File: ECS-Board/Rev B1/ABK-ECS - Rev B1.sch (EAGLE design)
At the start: 247 parts, among them J10 22-05-7068-06, J11 FTSH-105-01-L-DV-NOPASTE, J2 USB-B-S-RA, J21 FTSH-103-01-L-DV-NOPASTE, J4 MSTBA2, J5 22-05-7068-06, J6 22-05-7028-02, J7 22-05-7068-06, J8 22-05-7068-06, J9 22-05-7028-02, K1 G6K-2G-Y, SW1 B3FS-1015, SW2 B3FS-1015, T1 EXMACHINA-LOGO-NAME, T10 MMBT2222AL, T11 MMBT2222AL, T12 IRLML5103TRPBF, T13 IRLML5103TRPBF, T14 IRLML5103TRPBF, T15 IRLML5103TRPBF, T16 MMBT2222AL, T17 MMBT2222AL, T18 MMBT2222AL, T19 MMBT2222AL, T2 IRLML5103TRPBF, T20 MMBT2907ALT3, T3 MMBT2222AL, T4 IRLML5103TRPBF, T5 IRLML5103TRPBF, T6 IRLML5103TRPBF, T7 IRLML5103TRPBF, T8 MMBT2222AL, T9 MMBT2222AL, U1 AT24C512C-SSHM-B, U2 LPC1768FBD100, U3 LT3686HDDPBF, U4 LT3686HDDPBF, U6 CD4050BD, U7 CD4050BD, X1 FC-135, X2 ASE-12, X3 3000

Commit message: Place and route ethernet interface
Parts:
- removed D14: 1N4148WS, diode:1N4148WS
- removed J21: FTSH-103-01-L-DV-NOPASTE, con-samtec:FTSH-103-01-L-DV-NOPASTE
- added C20, C21: 0.1uF, rcl:C-EUC0603
- added C25, C27, C28, C29, C31, C32, C33, C34: 100nF, rcl:C-EUC0603
- added C26, C30: 10uF, rcl:CPOL-EUCT3216
- added D4: STPS3L40UF, diode:STPS3L40UF
- added J1: USB-B-S-RA, con-multicomp:USB-B-S-RA
- added J12: RB1-125BAG1A, con-wiznet:RB1-125BAG1A
- added J3: 22-05-7068-06, con-molex:22-05-7068-06
- added R124, R125: 220, rcl:R-EU_R0603
- added R126, R127, R128, R129: 49.9, rcl:R-EU_R0603
- added R130: 4K7, rcl:R-EU_R0603
- added R131: 2K2, rcl:R-EU_R0603
- added U5: CD4050BD, ti:CD4050BD
- added X4: ASE_50, crystal:ASE
- C1: value 10uF -> 0.1uF; device rcl:CPOL-EUCT3216 -> rcl:C-EUC0603; MPN F931A106MAA -> MC0603B104K160CT; OC_NEWARK 58R3260 -> 06R4923
- C10, C5: value 18pF -> 0.1uF; MPN GRM1885C1H180JA01D -> MC0603B104K160CT; OC_NEWARK 14T3328 -> 06R4923
- C23: value 0.1uF -> 4.7uF; device rcl:C-EUC0603 -> rcl:CPOL-EUCT3216; MPN MC0603B104K160CT -> F931A475MAA; OC_NEWARK 06R4923 -> 58R3271
- C24: value 0.1uF -> 100nF; MPN MC0603B104K160CT -> MC0603B104K250CT; OC_NEWARK 06R4923 -> 06R4925
- C3, C9: value 0.1uF -> 18pF; MPN MC0603B104K160CT -> GRM1885C1H180JA01D; OC_NEWARK 06R4923 -> 14T3328
- C4: value 0.1uF -> 10uF; device rcl:C-EUC0603 -> rcl:CPOL-EUCT3216; MPN MC0603B104K160CT -> F931A106MAA; OC_NEWARK 06R4923 -> 58R3260
- D5: value STPS3L40UF -> 1N4148WS; device diode:STPS3L40UF -> diode:1N4148WS; MPN (none) -> 1N4148WS; OC_NEWARK 06X0873 -> 31Y5518
- J10: value 22-05-7068-06 -> FTSH-105-01-L-DV-NOPASTE; device con-molex:22-05-7068-06 -> con-samtec:FTSH-105-01-L-DV-NOPASTE
- J11: value FTSH-105-01-L-DV-NOPASTE -> 22-05-7028-02; device con-samtec:FTSH-105-01-L-DV-NOPASTE -> con-molex:22-05-7028-02; MPN (none) -> 22-05-7028; OC_NEWARK (none) -> 25M1728
- J2: value USB-B-S-RA -> MSTBA2; device con-multicomp:USB-B-S-RA -> con-phoenix-508:MSTBA2; MPN USB-B-S-RA -> (none); OC_NEWARK 14N8154 -> (none)
- J4: value MSTBA2 -> 22-05-7028-02; device con-phoenix-508:MSTBA2 -> con-molex:22-05-7028-02; MPN (none) -> 22-05-7028; OC_NEWARK (none) -> 25M1728
- J6: value 22-05-7028-02 -> 22-05-7068-06; device con-molex:22-05-7028-02 -> con-molex:22-05-7068-06; MPN 22-05-7028 -> (none); OC_NEWARK 25M1728 -> (none)
- J8: value 22-05-7068-06 -> 22-05-7028-02; device con-molex:22-05-7068-06 -> con-molex:22-05-7028-02; MPN (none) -> 22-05-7028; OC_NEWARK (none) -> 25M1728
- J9: value 22-05-7028-02 -> FTSH-103-01-L-DV-NOPASTE; device con-molex:22-05-7028-02 -> con-samtec:FTSH-103-01-L-DV-NOPASTE; MPN 22-05-7028 -> (none); OC_NEWARK 25M1728 -> (none)
- R5: value 1K -> 39K; device rcl:R-EU_R1206 -> rcl:R-EU_R0603
- R6: value 33 -> 24K; MPN RC0603FR-0733RL -> (none); OC_NEWARK 68R0085 -> (none)
- R64: value 10K -> 1K; device rcl:R-EU_R0603 -> rcl:R-EU_R1206; MPN RC0603FR-0710KL -> (none); OC_NEWARK 68R0049 -> (none)
- R65: value 100 -> 1K; device rcl:R-EU_R0603 -> rcl:R-EU_R1206; MPN RC0603FR-13100RL -> (none); OC_NEWARK 68R0131 -> (none)
- R67, R68, R69: value 1K -> 10K; device rcl:R-EU_R1206 -> rcl:R-EU_R0603; MPN (none) -> RC0603FR-0710KL; OC_NEWARK (none) -> 68R0049
- R71, R72, R73: value 10K -> 1K; MPN RC0603FR-0710KL -> RC0603FR-071KL; OC_NEWARK 68R0049 -> 68R0042
- R75, R76, R77: value 1K -> 1K5; MPN RC0603FR-071KL -> RC0603FR-071K5L; OC_NEWARK 68R0042 -> 68R0045
- R79, R80, R81: value 1K5 -> 4K7; MPN RC0603FR-071K5L -> RC0603FR-074K7L; OC_NEWARK 68R0045 -> 68R0092
- R8: value 24K -> 33; MPN (none) -> RC0603FR-0733RL; OC_NEWARK (none) -> 68R0085
- R83, R84, R85: value 4K7 -> 100; MPN RC0603FR-074K7L -> RC0603FR-13100RL; OC_NEWARK 68R0092 -> 68R0131
- R87, R88, R89: value 100 -> 330; MPN RC0603FR-13100RL -> RC0603FR-07330RL; OC_NEWARK 68R0131 -> 98K7391
- R91: value 330 -> 1K; device rcl:R-EU_R0603 -> rcl:R-EU_R1206; MPN RC0603FR-07330RL -> (none); OC_NEWARK 98K7391 -> (none)
- R92: value 330 -> 10K; MPN RC0603FR-07330RL -> RC0603FR-0710KL; OC_NEWARK 98K7391 -> 68R0049
- R93: value 330 -> 100; MPN RC0603FR-07330RL -> RC0603FR-13100RL; OC_NEWARK 98K7391 -> 68R0131
- R97: value 39K -> 1K; device rcl:R-EU_R0603 -> rcl:R-EU_R1206
- T1: value EXMACHINA-LOGO-NAME -> MMBT2907ALT3; device exmachina:EXMACHINA-LOGO-NAME -> transistor:MMBT2907ALT3; OC_NEWARK unknown -> (none)
- T11, T16, T3: value MMBT2222AL -> IRLML5103TRPBF; device transistor:MMBT2222AL -> International_Rectifier_By_element14_Batch_1:IRLML5103TRPBF; MF ON SEMICONDUCTOR -> INTERNATIONAL RECTIFIER(IR); MPN MMBT2222ALT1G -> IRLML5103TRPBF; OC_NEWARK 84K8795 -> 63J7612
- T12, T7: value IRLML5103TRPBF -> MMBT2222AL; device International_Rectifier_By_element14_Batch_1:IRLML5103TRPBF -> transistor:MMBT2222AL; MF INTERNATIONAL RECTIFIER(IR) -> ON SEMICONDUCTOR; MPN IRLML5103TRPBF -> MMBT2222ALT1G; OC_NEWARK 63J7612 -> 84K8795
- T2: value IRLML5103TRPBF -> EXMACHINA-LOGO-NAME; device International_Rectifier_By_element14_Batch_1:IRLML5103TRPBF -> exmachina:EXMACHINA-LOGO-NAME; MF INTERNATIONAL RECTIFIER(IR) -> (none); MPN IRLML5103TRPBF -> (none); OC_NEWARK 63J7612 -> unknown
- T20: value MMBT2907ALT3 -> MMBT2222AL; device transistor:MMBT2907ALT3 -> transistor:MMBT2222AL; MF (none) -> ON SEMICONDUCTOR; MPN (none) -> MMBT2222ALT1G; OC_NEWARK (none) -> 84K8795
- TC1: value TC2050-IDC-NL -> TC2030-IDC-NL; device TagConnect:TC2050-IDC-NL -> TagConnect:TC2030-IDC-NL
- TC2: value TC2030-IDC-NL -> TC2050-IDC-NL; device TagConnect:TC2030-IDC-NL -> TagConnect:TC2050-IDC-NL
- U7: value CD4050BD -> DP83848JSQ/NOPB; device ti:CD4050BD -> textas:DP83848JSQ/NOPB; MPN (none) -> DP83848JSQ/NOPB; OC_NEWARK (none) -> 96W2841
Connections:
- removed net N$75 (its old number): LED17.A, R74.1, R82.1, R86.1
- removed net N$76 (its old number): OK3A.EMIT, R86.2
- removed net N$79 (its old number): LED18.A, R75.1, R83.1, R87.1
- removed net N$80 (its old number): OK3B.EMIT, R87.2
- removed net N$83 (its old number): LED19.A, R76.1, R84.1, R88.1
- removed net N$86 (its old number): LED20.A, R77.1, R85.1, R89.1
- removed net N$87 (its old number): OK3C.EMIT, R88.2
- removed net N$88 (its old number): OK3D.EMIT, R89.2
- removed net N$89 (its old number): OK3A.A, R90.1
- removed net N$91 (its old number): OK3B.A, R91.1
- removed net N$92 (its old number): OK3D.A, R93.1
- removed net N$93 (its old number): OK3C.A, R92.1
- removed net N$94 (its old number): LED17.C, R78.1
- removed net N$95 (its old number): LED18.C, R79.1
- removed net N$96 (its old number): LED19.C, R80.1
- removed net N$97 (its old number): LED20.C, R81.1
- new net AGND: J12.P$1
- new net ETH_CRS: U2.P1[8]/ENET_CRS, U7.CRS/CRS_DV/LED_CFG
- new net ETH_MDC: U2.P1[16]/ENET_MDC, U7.MDC
- new net ETH_MDIO: U2.P1[17]/ENET_MDIO, U7.MDIO
- new net ETH_RST: U7.RESET_N
- new net ETH_RXD_0: U2.P1[9]/ENET_RXD0, U7.RXD_0/PHYAD1
- new net ETH_RXD_1: U2.P1[10]/ENET_RXD1, U7.RXD_1/PHYAD2
- new net ETH_RX_ER: U2.P1[14]/ENET_RX_ER, U7.RX_ER/MDIX_EN
- new net ETH_RX_N: J12.RD-, R129.2, U7.RD-
- new net ETH_RX_P: J12.RD+, R128.2, U7.RD+
- new net ETH_TXD_0: U2.P1[0]/ENET_TXD0, U7.TXD_0
- new net ETH_TXD_1: U2.P1[1]/ENET_TXD1, U7.TXD_1
- new net ETH_TXD_EN: U2.P1[4]/ENET_TX_EN, U7.TX_EN
- new net ETH_TX_N: J12.TD-, R127.2, U7.TD-
- new net ETH_TX_P: J12.TD+, R126.2, U7.TD+
- new net ETH_X1: U2.P1[15]/ENET_REF_CLK, U7.X1, X4.OUT
- new net L1_1: J12.L2, U7.LED_LINK/AN0
- new net L1_2: J12.L4, U7.LED_SPEED/AN1
- new net MII_MODE: R131.2, U7.RX_DV/MII_MODE
- new net N$113: J12.L1, R124.1
- new net N$115: J12.L3, R125.1
- new net N$116: R130.1, U7.RBIAS
- new net N$31: LED17.A, R71.1, R79.1, R83.1
- new net N$33: OK3A.EMIT, R83.2
- new net N$34: LED18.A, R72.1, R80.1, R84.1
- new net N$35: OK3B.EMIT, R84.2
- new net N$36: LED19.A, R73.1, R81.1, R85.1
- new net N$37: LED20.A, R74.1, R82.1, R86.1
- new net N$38: OK3C.EMIT, R85.2
- new net N$39: OK3D.EMIT, R86.2
- new net N$40: OK3A.A, R87.1
- new net N$42: OK3B.A, R88.1
- new net N$43: OK3D.A, R90.1
- new net N$46: OK3C.A, R89.1
- new net N$66: LED17.C, R75.1
- new net N$67: LED18.C, R76.1
- new net N$68: LED19.C, R77.1
- new net N$69: LED20.C, R78.1
- new net PFBOUT: C26.+, C27.1, C28.1, C29.1, U7.PFBIN1, U7.PFBIN2, U7.PFBOUT
- net !ISP_BOOT: now also J9-2.S, TC1.2; no longer J21-2.S, TC2.2
- net !ISP_RST: now also J9-6.S, TC1.6; no longer J21-6.S, TC2.6
- net !RESET: now also J10-10.S, TC2.10; no longer J11-10.S, TC1.10
- net +24V: now also J3-1.S, J4-1.S, R67.2, R68.2, R69.2, R92.2, T11.S, T16.S, T3.S; no longer J10-1.S, J8-1.S, R64.2, R71.2, R72.2, R73.2, T12.S, T2.S, T7.S
- net +3V3: now also C1.1, C10.1, C21.1, C22.1, C23.+, C25.1, C30.+, C31.1, C32.1, C33.1, C34.1, C4.+, C5.1, J10-1.S, J12.CT, J9-1.S, R124.2, R125.2, R126.1, R127.1, R128.1, R129.1, R131.1, T1.C, U5.VCC, U7.AVDD33, U7.IOVDD33, U7.IOVDD33_2, X4.TRI, X4.VDD; no longer C1.+, C23.1, C3.1, C4.1, C9.1, J11-1.S, J21-1.S, T20.C, U7.VCC
- net +5V: now also J11-1.S
- net GND: now also C1.2, C20.2, C21.2, C23.-, C25.2, C26.-, C27.2, C28.2, C29.2, C30.-, C31.2, C32.2, C33.2, C34.2, C4.-, D4.A, D5.2, J1.GND, J10-3.S, J10-5.S, J10-7.S, J10-9.S, J11-2.S, J12.R4, J12.R5, J12.R6, J2-2.1, J3-6.S, J6-6.S, J8-2.S, J9-5.S, R130.2, R64.1, R65.1, R75.2, R76.2, R77.2, R91.1, T12.E, T20.E, T7.E, TC2.3, TC2.7, TC2.9, U5.VSS, U7.AGND, U7.AGND_2, U7.DAP, U7.DGND, U7.IOGND, X4.GND; no longer C1.-, C23.2, C4.2, D14.2, D5.A, J10-6.S, J11-3.S, J11-5.S, J11-7.S, J11-9.S, J2.GND, J21-5.S, J4-2.1, J8-6.S, J9-2.S, R67.1, R68.1, R69.1, R83.2, R84.2, R85.2, T11.E, T16.E, T3.E, TC1.3, TC1.7, TC1.9, U7.VSS
- net INPUT1.1: now also U6.D; no longer U7.D
- net INPUT1.1_MCU: now also U6.J=D; no longer U7.J=D
- net INPUT1.2: now also U6.E; no longer U7.E
- net INPUT1.2_MCU: now also U6.K=E; no longer U7.K=E
- net INPUT1.3: now also U6.B; no longer U7.B
- net INPUT1.3_MCU: now also U6.H=B; no longer U7.H=B
- net INPUT1.4: now also U6.A; no longer U7.A
- net INPUT1.4_MCU: now also U6.G=A; no longer U7.G=A
- net INPUT2.1: now also U5.E; no longer U6.E
- net INPUT2.1_MCU: now also U5.K=E; no longer U6.K=E
- net INPUT2.2: now also U5.D; no longer U6.D
- net INPUT2.2_MCU: now also U5.J=D; no longer U6.J=D
- net INPUT2.3: now also U5.B; no longer U6.B
- net INPUT2.3_MCU: now also U5.H=B; no longer U6.H=B
- net INPUT2.4: now also U5.A; no longer U6.A
- net INPUT2.4_MCU: now also U5.G=A; no longer U6.G=A
- net INPUT3.1: now also C20.1, U5.F; no longer C22.1, U6.F
- net INPUT3.1_MCU: now also U5.L=F; no longer U6.L=F
- net ISP_RXDO: now also J9-4.S, TC1.4; no longer J21-4.S, TC2.4
- net ISP_TXDO: now also J9-3.S, TC1.3; no longer J21-3.S, TC2.3
- net JTAG_TCK: now also J10-4.S, TC2.4; no longer J11-4.S, TC1.4
- net JTAG_TDI: now also J10-8.S, TC2.8; no longer J11-8.S, TC1.8
- net JTAG_TDO: now also J10-6.S, TC2.6; no longer J11-6.S, TC1.6
- net JTAG_TMS: now also J10-2.S, TC2.2; no longer J11-2.S, TC1.2
- net MOTOR_VFQ: now also D9.1, J8-1.S, R91.2, T11.D; no longer D6.1, J9-1.S, R68.2, T2.D
- net N$1: now also J1.DATA+, R8.1; no longer J2.DATA+, R7.1
- net N$102: now also J5-4.S; no longer J7-4.S
- net N$105: now also J5-3.S; no longer J7-3.S
- net N$112: now also J5-2.S; no longer J7-2.S
- net N$114: now also J1.VUSB, R6.2; no longer J2.VUSB, R8.2
- net N$17: now also R102.2, T17.B; no longer R74.2, T8.B
- net N$18: now also R98.1, T13.G, T17.C; no longer R70.1, T4.G, T8.C
- net N$19: now also R103.2, T18.B; no longer R75.2, T9.B
- net N$2: now also J1.DATA-, R7.1; no longer J2.DATA-, R6.1
- net N$20: now also R99.1, T14.G, T18.C; no longer R71.1, T5.G, T9.C
- net N$21: now also R104.2, T19.B; no longer R76.2, T10.B
- net N$22: now also R100.1, T15.G, T19.C; no longer R72.1, T10.C, T6.G
- net N$23: now also R105.2, T20.B; no longer R77.2, T11.B
- net N$24: now also R101.1, T16.G, T20.C; no longer R73.1, T11.C, T7.G
- net N$25: now also R93.1, T12.B; no longer R65.1, T3.B
- net N$26: now also R92.1, T11.G, T12.C; no longer R64.1, T2.G, T3.C
- net N$28: now also D4.C; no longer D5.C
- net N$30: now also T1.E; no longer T20.E
- net N$32: now also J4-2.S; no longer J6-2.S
- net N$52: now also J3-2.S; no longer J5-2.S
- net N$53: now also J3-3.S; no longer J5-3.S
- net N$54: now also J3-4.S; no longer J5-4.S
- net N$55: now also J3-5.S; no longer J5-5.S
- net N$70: now also J1.SHL; no longer J2.SHL
- net N$71: now also R67.1, T3.G, T7.C; no longer R98.1, T12.G, T16.C
- net N$72: now also R68.1, T4.G, T8.C; no longer R99.1, T13.G, T17.C
- net N$77: now also R69.1, T5.G, T9.C; no longer R100.1, T14.G, T18.C
- net N$78: now also R70.1, T10.C, T6.G; no longer R101.1, T15.G, T19.C
- net N$82: now also J5-5.S; no longer J7-5.S
- net N$84: now also R71.2, T7.B; no longer R102.2, T16.B
- net N$85: now also R72.2, T8.B; no longer R103.2, T17.B
- net N$98: now also R73.2, T9.B; no longer R104.2, T18.B
- net N$99: now also R74.2, T10.B; no longer R105.2, T19.B
- net OUTPUT1.1: now also D5.1, J6-2.S, R63.2, T3.D; no longer D11.1, J10-2.S, R96.2, T12.D
- net OUTPUT1.1_MCU: now also R87.2; no longer R118.2
- net OUTPUT1.2: now also D6.1, J6-3.S, R64.2, T4.D; no longer D12.1, J10-3.S, R95.2, T13.D
- net OUTPUT1.2_MCU: now also R88.2; no longer R119.2
- net OUTPUT1.3: now also D7.1, J6-4.S, R65.2, T5.D; no longer D13.1, J10-4.S, R94.2, T14.D
- net OUTPUT1.3_MCU: now also R89.2; no longer R120.2
- net OUTPUT1.4: now also D8.1, J6-5.S, R66.2, T6.D; no longer D14.1, J10-5.S, R69.2, T15.D
- net OUTPUT1.4_MCU: now also R90.2; no longer R121.2
- net OUTPUT2.1: now also D10.1, J7-2.S, R94.2, T13.D; no longer D7.1, J8-2.S, R5.2, T4.D
- net OUTPUT2.1_MCU: now also R118.2; no longer R90.2
- net OUTPUT2.2: now also D11.1, J7-3.S, R95.2, T14.D; no longer D8.1, J8-3.S, R63.2, T5.D
- net OUTPUT2.2_MCU: now also R119.2; no longer R91.2
- net OUTPUT2.3: now also D12.1, J7-4.S, R96.2, T15.D; no longer D9.1, J8-4.S, R66.2, T6.D
- net OUTPUT2.3_MCU: now also R120.2; no longer R92.2
- net OUTPUT2.4: now also D13.1, J7-5.S, R97.2, T16.D; no longer D10.1, J8-5.S, R67.2, T7.D
- net OUTPUT2.4_MCU: now also R121.2; no longer R93.2
- net OUTPUT3.2_MCU: now also R93.2; no longer R65.2
- net RTCX1: now also C3.1; no longer C5.1
- net RTCX2: now also C9.1; no longer C10.1
- net USB_CONNECT: now also T1.B; no longer T20.B
- net USB_D_N: now also R7.2; no longer R6.2
- net USB_D_P: now also R8.2; no longer R7.2
- net USB_V_BUS: now also R5.2, R6.1; no longer R8.1, R97.2
- net VIN: now also J2-1.1; no longer J4-1.1
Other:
- note added: "ETHERNET INPUT"
- note added: "ETHERNETPHI"

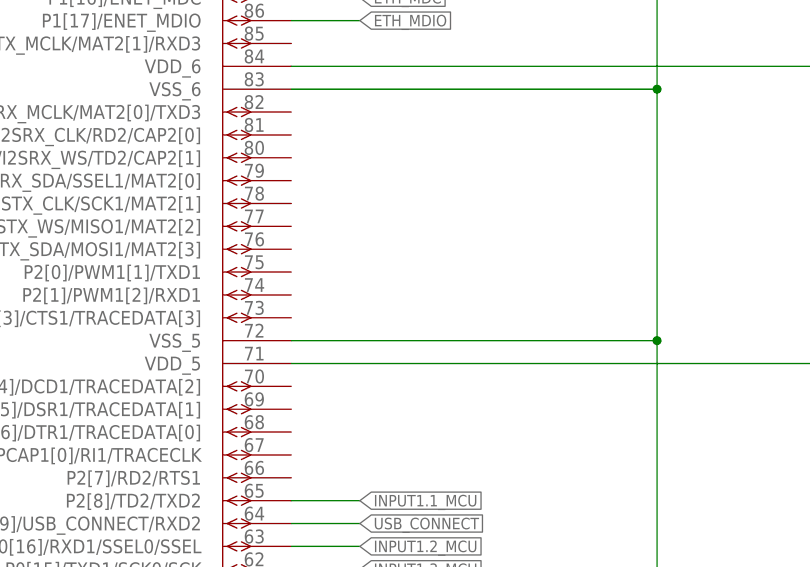
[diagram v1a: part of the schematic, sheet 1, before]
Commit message: Route JTAG, ISCP and LED On board
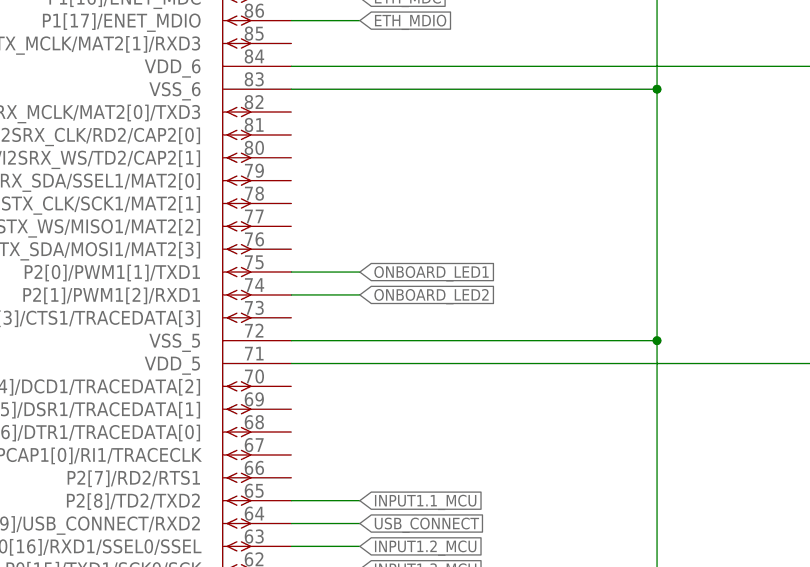
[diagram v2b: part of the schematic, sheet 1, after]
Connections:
- net ONBOARD_LED1: now also U2.P2[0]/PWM1[1]/TXD1
- net ONBOARD_LED2: now also U2.P2[1]/PWM1[2]/RXD1
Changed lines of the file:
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@@
 <wire x1="370.84" y1="66.04" x2="370.84" y2="58.42" width="0.1524" layer="91"/>
+</segment>
+<segment>
+<wire x1="325.12" y1="170.18" x2="317.5" y2="170.18" width="0.1524" layer="91"/>
+<pinref part="U2" gate="A" pin="P2[0]/PWM1[1]/TXD1"/>
+<label x="325.12" y="170.18" size="1.27" layer="95" xref="yes"/>
 </segment>
 </net>
@@
 <label x="127" y="147.32" size="1.27" layer="95" rot="R180" xref="yes"/>
 </segment>
+<segment>
+<wire x1="325.12" y1="167.64" x2="317.5" y2="167.64" width="0.1524" layer="91"/>
+<pinref part="U2" gate="A" pin="P2[1]/PWM1[2]/RXD1"/>
+<label x="325.12" y="167.64" size="1.27" layer="95" xref="yes"/>
+</segment>
 </net>

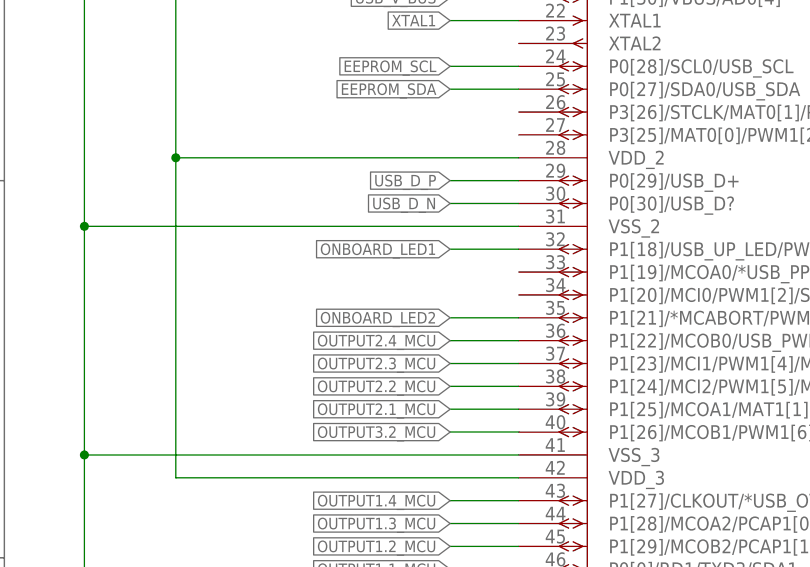
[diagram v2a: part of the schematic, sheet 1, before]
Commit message: Route ethernet LED and Reset signal
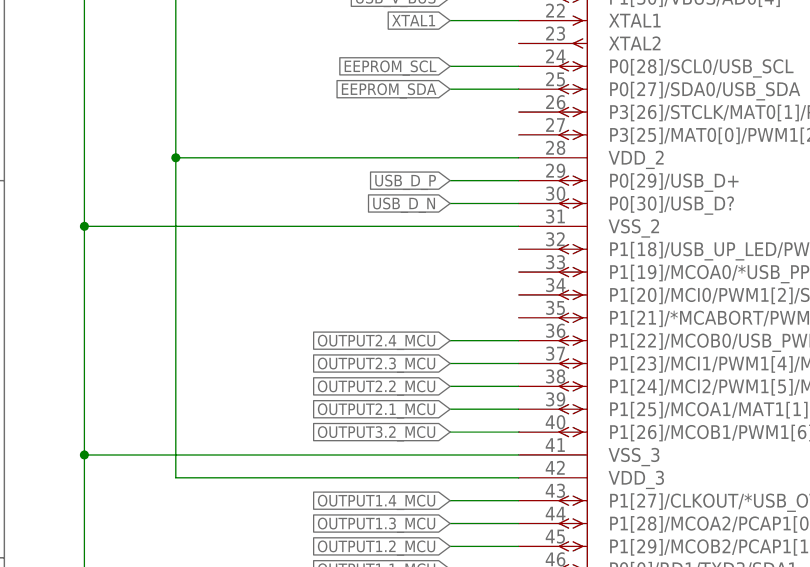
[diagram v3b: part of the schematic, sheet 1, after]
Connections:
- net ONBOARD_LED1: no longer U2.P1[18]/USB_UP_LED/PWM1[1]/CAP1[0]
- net ONBOARD_LED2: no longer U2.P1[21]/*MCABORT/PWM1[3]/SSEL0
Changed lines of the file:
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@@
 <net name="ONBOARD_LED1" class="1">
-<segment>
-<pinref part="U2" gate="A" pin="P1[18]/USB_UP_LED/PWM1[1]/CAP1[0]"/>
-<wire x1="134.62" y1="154.94" x2="127" y2="154.94" width="0.1524" layer="91"/>
-<label x="127" y="154.94" size="1.27" layer="95" rot="R180" xref="yes"/>
-</segment>
 <segment>
 <label x="358.14" y="66.04" size="1.27" layer="95" rot="R180" xref="yes"/>
@@
 </segment>
 <segment>
-<wire x1="134.62" y1="147.32" x2="127" y2="147.32" width="0.1524" layer="91"/>
-<pinref part="U2" gate="A" pin="P1[21]/*MCABORT/PWM1[3]/SSEL0"/>
-<label x="127" y="147.32" size="1.27" layer="95" rot="R180" xref="yes"/>
-</segment>
-<segment>

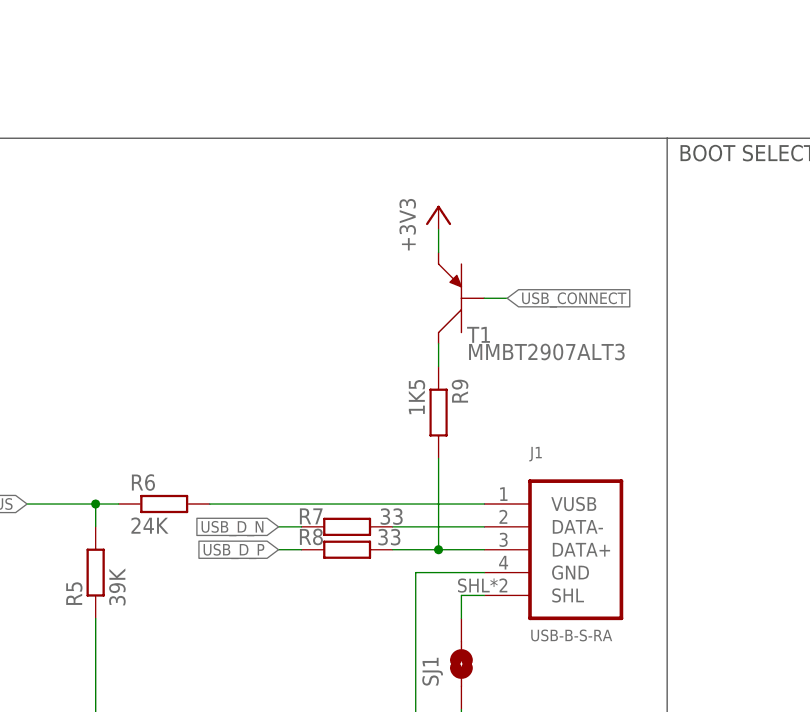
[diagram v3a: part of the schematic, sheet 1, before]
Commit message: Add 0R to the USB Pull-up
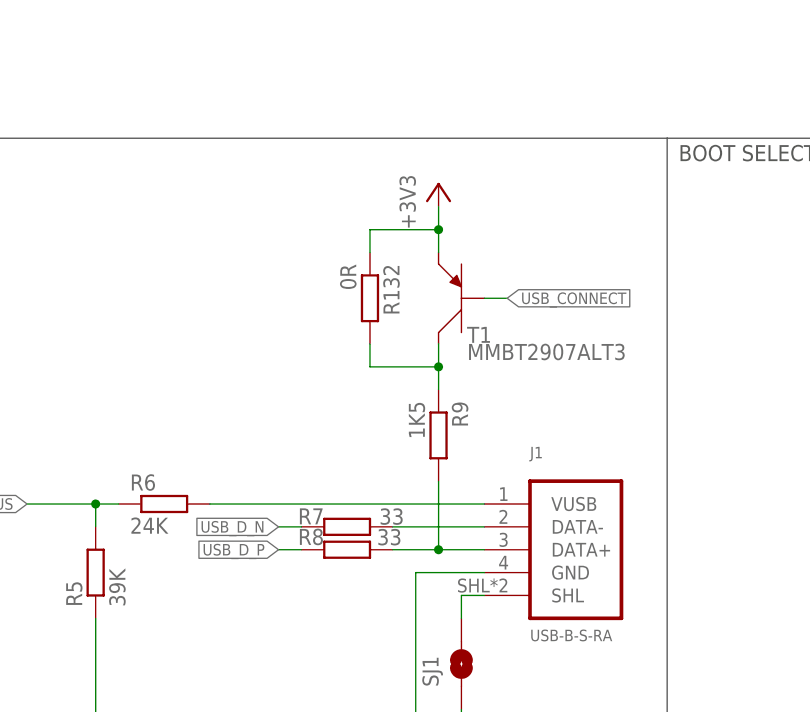
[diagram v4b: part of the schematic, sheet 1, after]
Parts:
- added R132: 0R, rcl:R-EU_R0603
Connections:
- net +3V3: now also R132.1
- net N$30: now also R132.2
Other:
- moved on the sheet: R9
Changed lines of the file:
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@@
 <part name="GND123" library="supply1" deviceset="GND" device=""/>
 <part name="P+46" library="supply1" deviceset="+5V" device=""/>
+<part name="R132" library="rcl" deviceset="R-EU_" device="R0603" value="0R">
+<attribute name="MF" value=""/>
+<attribute name="MPN" value="RC0603FR-070RL"/>
+<attribute name="OC_NEWARK" value="50Y7761"/>
+</part>
 </parts>
 <sheets>
@@
 </instance>
 <instance part="GND12" gate="1" x="180.34" y="12.7"/>
-<instance part="R9" gate="G$1" x="182.88" y="50.8" rot="R270">
-<attribute name="OC_NEWARK" x="182.88" y="50.8" size="1.778" layer="96" display="off"/>
-<attribute name="MF" x="182.88" y="50.8" size="1.778" layer="96" display="off"/>
-<attribute name="MPN" x="182.88" y="50.8" size="1.778" layer="96" display="off"/>
-</instance>
-<instance part="+3V311" gate="G$1" x="182.88" y="73.66"/>
+<instance part="R9" gate="G$1" x="182.88" y="48.26" rot="R270">
+<attribute name="OC_NEWARK" x="182.88" y="48.26" size="1.778" layer="96" display="off"/>
+<attribute name="MF" x="182.88" y="48.26" size="1.778" layer="96" display="off"/>
+<attribute name="MPN" x="182.88" y="48.26" size="1.778" layer="96" display="off"/>
+</instance>
+<instance part="+3V311" gate="G$1" x="182.88" y="76.2"/>
 <instance part="LED2" gate="G$1" x="370.84" y="55.88">
 <attribute name="OC_NEWARK" x="370.84" y="55.88" size="1.778" layer="96" display="off"/>
@@
 <instance part="R5" gate="G$1" x="144.78" y="33.02" rot="R90"/>
 <instance part="GND11" gate="1" x="144.78" y="12.7"/>
+<instance part="R132" gate="G$1" x="175.26" y="63.5" rot="R270">
+<attribute name="OC_NEWARK" x="175.26" y="63.5" size="1.778" layer="96" rot="R90" display="off"/>
+<attribute name="MF" x="175.26" y="63.5" size="1.778" layer="96" rot="R90" display="off"/>
+<attribute name="MPN" x="175.26" y="63.5" size="1.778" layer="96" rot="R90" display="off"/>
+</instance>
 </instances>
 <busses>
@@
 <pinref part="+3V311" gate="G$1" pin="+3V3"/>
 <wire x1="182.88" y1="68.58" x2="182.88" y2="71.12" width="0.1524" layer="91"/>
+<pinref part="R132" gate="G$1" pin="1"/>
+<wire x1="182.88" y1="71.12" x2="182.88" y2="73.66" width="0.1524" layer="91"/>
+<wire x1="182.88" y1="71.12" x2="175.26" y2="71.12" width="0.1524" layer="91"/>
+<wire x1="175.26" y1="71.12" x2="175.26" y2="68.58" width="0.1524" layer="91"/>
+<junction x="182.88" y="71.12"/>
 </segment>
 </net>
@@
 <pinref part="R9" gate="G$1" pin="2"/>
 <wire x1="182.88" y1="35.56" x2="187.96" y2="35.56" width="0.1524" layer="91"/>
-<wire x1="182.88" y1="35.56" x2="182.88" y2="45.72" width="0.1524" layer="91"/>
+<wire x1="182.88" y1="35.56" x2="182.88" y2="43.18" width="0.1524" layer="91"/>
 <junction x="182.88" y="35.56"/>
 <pinref part="J1" gate="G$1" pin="DATA+"/>
@@
 <pinref part="R9" gate="G$1" pin="1"/>
 <wire x1="182.88" y1="58.42" x2="182.88" y2="55.88" width="0.1524" layer="91"/>
-</segment>
-</net>
+<pinref part="R132" gate="G$1" pin="2"/>
+<wire x1="182.88" y1="55.88" x2="182.88" y2="53.34" width="0.1524" layer="91"/>
+<wire x1="182.88" y1="55.88" x2="175.26" y2="55.88" width="0.1524" layer="91"/>
+<wire x1="175.26" y1="55.88" x2="175.26" y2="58.42" width="0.1524" layer="91"/>
+<junction x="182.88" y="55.88"/>
+</segment>
+</net>

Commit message: Routing improvement
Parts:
- R132: value 0R -> 0R, DNI
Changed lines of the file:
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@@
 <part name="GND123" library="supply1" deviceset="GND" device=""/>
 <part name="P+46" library="supply1" deviceset="+5V" device=""/>
-<part name="R132" library="rcl" deviceset="R-EU_" device="R0603" value="0R">
+<part name="R132" library="rcl" deviceset="R-EU_" device="R0603" value="0R, DNI">
 <attribute name="MF" value=""/>
 <attribute name="MPN" value="RC0603FR-070RL"/>
